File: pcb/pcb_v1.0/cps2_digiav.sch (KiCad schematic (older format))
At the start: 47 parts, among them U31 74LVC245, U32 74LVC245, U33 74LVC245, U34 SN74LVC3G17, U7 TC1262-3.3VDBTR, U8 TLV70033

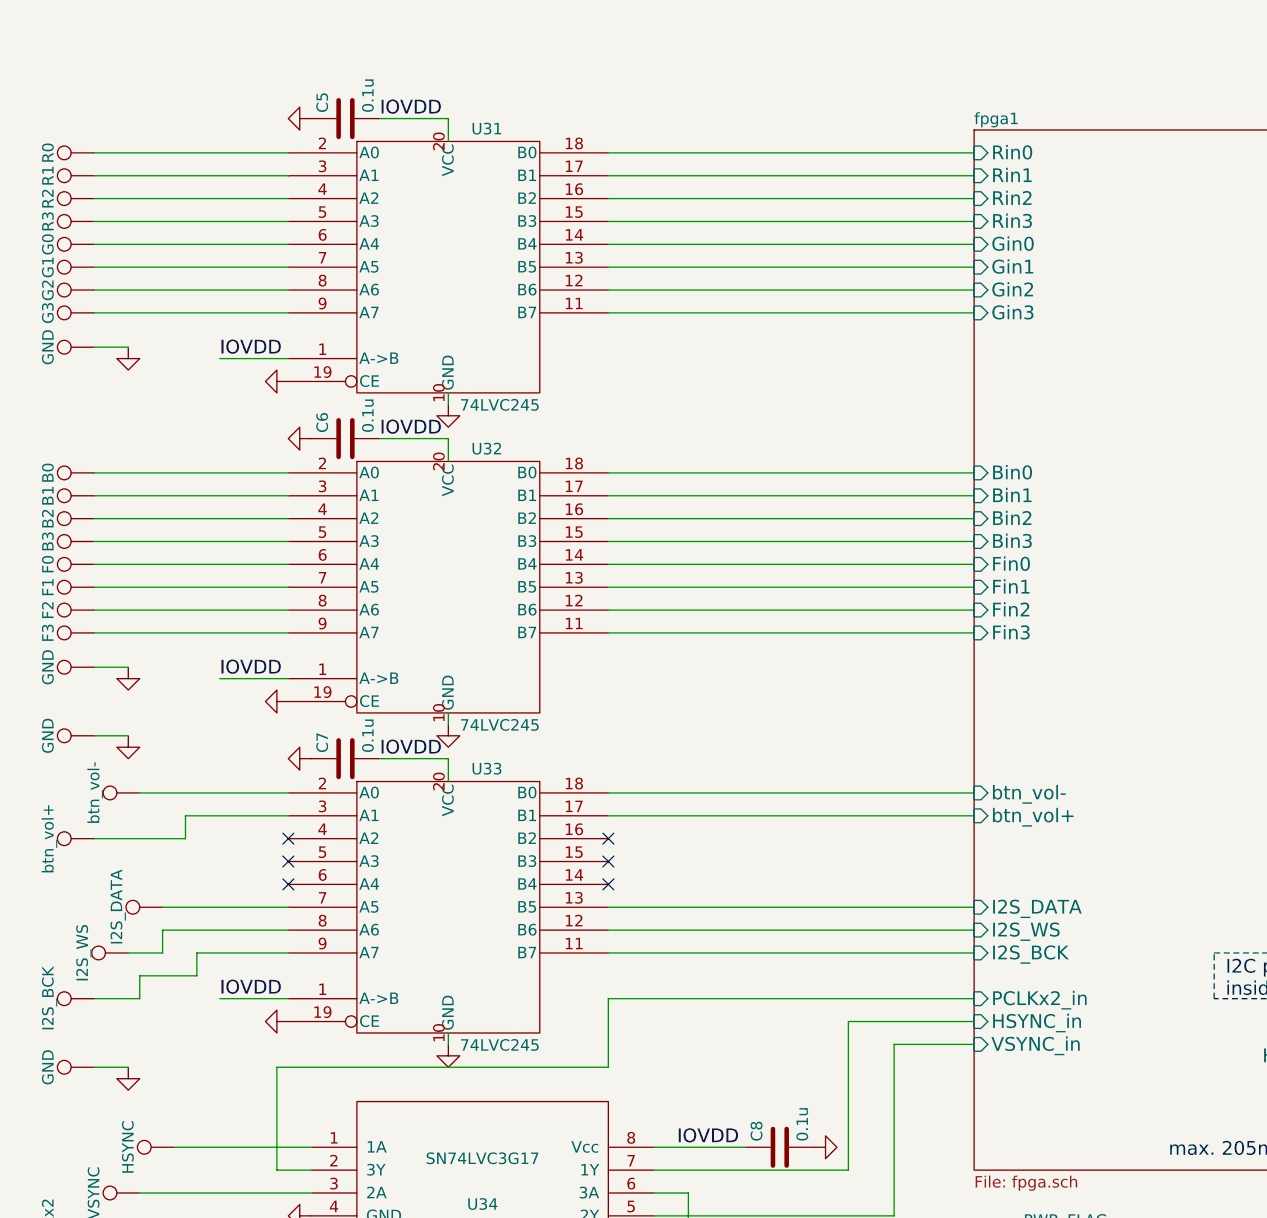
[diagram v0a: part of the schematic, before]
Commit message: Moved ICs to top, made to fit ontop of CPS2 DIPs
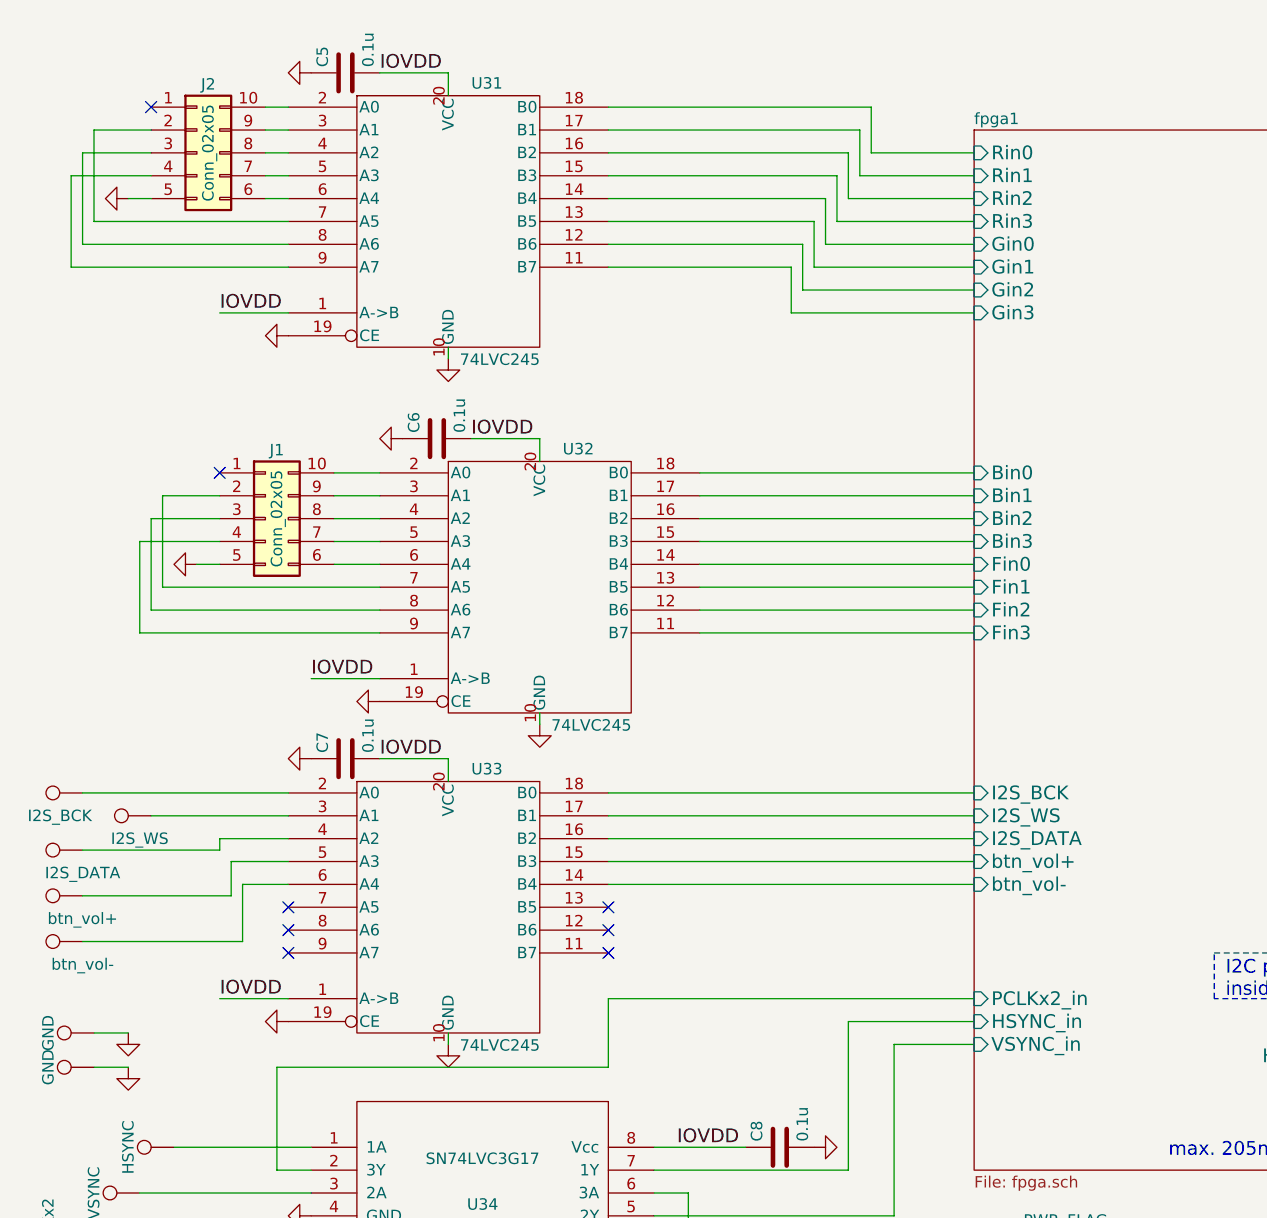
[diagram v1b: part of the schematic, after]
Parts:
- removed W10: G3, custom_components:SMD_PAD, symbol TEST_1P
- removed W11: B0, custom_components:SMD_PAD, symbol TEST_1P
- removed W12: B1, custom_components:SMD_PAD, symbol TEST_1P
- removed W13: B2, custom_components:SMD_PAD, symbol TEST_1P
- removed W14: B3, custom_components:SMD_PAD, symbol TEST_1P
- removed W15: F0, custom_components:SMD_PAD, symbol TEST_1P
- removed W16: F1, custom_components:SMD_PAD, symbol TEST_1P
- removed W17: F2, custom_components:SMD_PAD, symbol TEST_1P
- removed W18: F3, custom_components:SMD_PAD, symbol TEST_1P
- removed W27, W28: GND, custom_components:SMD_PAD, symbol TEST_1P
- removed W3: R0, custom_components:SMD_PAD, symbol TEST_1P
- removed W4: R1, custom_components:SMD_PAD, symbol TEST_1P
- removed W5: R2, custom_components:SMD_PAD, symbol TEST_1P
- removed W6: R3, custom_components:SMD_PAD, symbol TEST_1P
- removed W7: G0, custom_components:SMD_PAD, symbol TEST_1P
- removed W8: G1, custom_components:SMD_PAD, symbol TEST_1P
- removed W9: G2, custom_components:SMD_PAD, symbol TEST_1P
- added J1, J2: Conn_02x05, Housings_DIP:DIP-10_W7.62mm_LongPads, symbol Conn_02x05_Counter_Clockwise
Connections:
- net GND: now also J1.5 (Pin_5), J2.5 (Pin_5)
- net fpga1/I2S_BCK: now also U33.18 (B0); no longer U33.11 (B7)
- net fpga1/I2S_DATA: now also U33.16 (B2); no longer U33.13 (B5)
- net fpga1/I2S_WS: now also U33.17 (B1); no longer U33.12 (B6)
- net fpga1/btn_vol+: now also U33.15 (B3); no longer U33.17 (B1)
- net fpga1/btn_vol-: now also U33.14 (B4); no longer U33.18 (B0)
- net at U31.2 (A0): now also J2.10 (Pin_10)
- net at U31.3 (A1): now also J2.9 (Pin_9)
- net at U31.4 (A2): now also J2.8 (Pin_8)
- net at U31.5 (A3): now also J2.7 (Pin_7)
- net at U31.6 (A4): now also J2.6 (Pin_6)
- net at U31.7 (A5): now also J2.2 (Pin_2)
- net at U31.8 (A6): now also J2.3 (Pin_3)
- net at U31.9 (A7): now also J2.4 (Pin_4)
- net at U32.2 (A0): now also J1.10 (Pin_10)
- net at U32.3 (A1): now also J1.9 (Pin_9)
- net at U32.4 (A2): now also J1.8 (Pin_8)
- net at U32.5 (A3): now also J1.7 (Pin_7)
- net at U32.6 (A4): now also J1.6 (Pin_6)
- net at U32.7 (A5): now also J1.2 (Pin_2)
- net at U32.8 (A6): now also J1.3 (Pin_3)
- net at U32.9 (A7): now also J1.4 (Pin_4)
- net at U33.2 (A0): now also W20.1; no longer W23.1
- net at U33.3 (A1): now also W22.1; no longer W19.1
- net at U33.4 (A2): now also W25.1
- net at U33.5 (A3): now also W19.1
- net at U33.6 (A4): now also W23.1
- net at U33.7 (A5): no longer W25.1
- net at U33.8 (A6): no longer W22.1
- net at U33.9 (A7): no longer W20.1
- no-connect marks 6 -> 8
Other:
- moved on the sheet: C5, C6, U31, U32

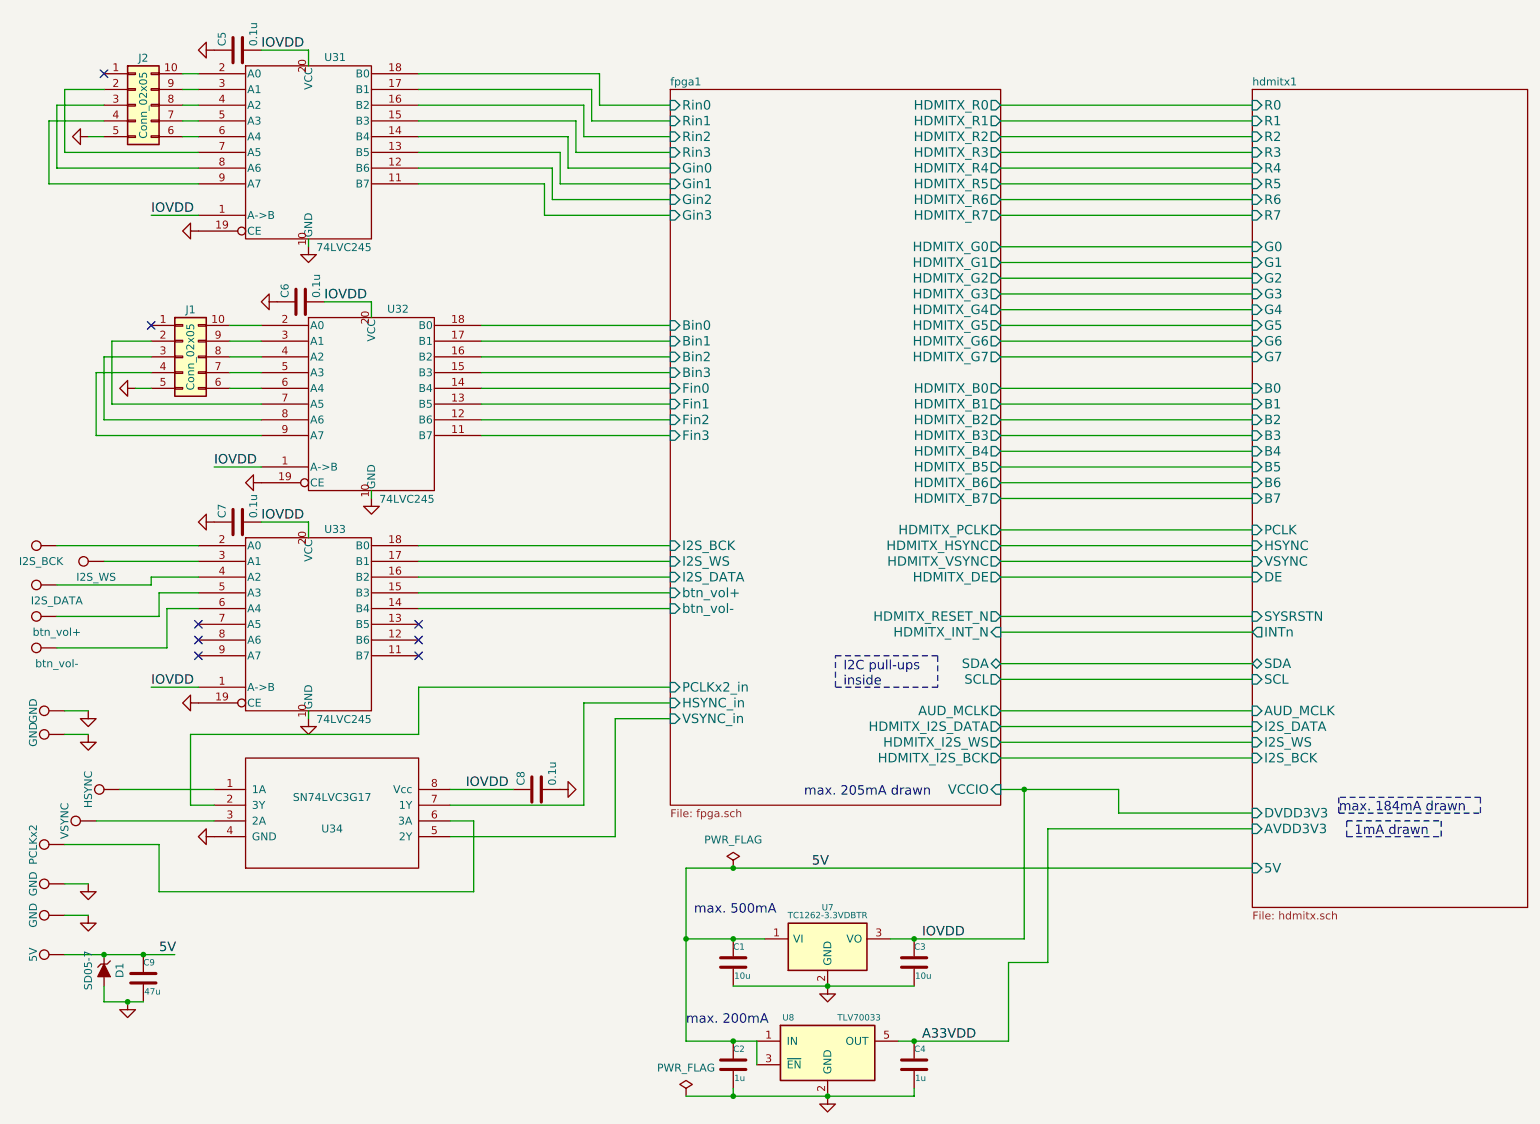
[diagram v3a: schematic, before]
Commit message: Added Si5351C
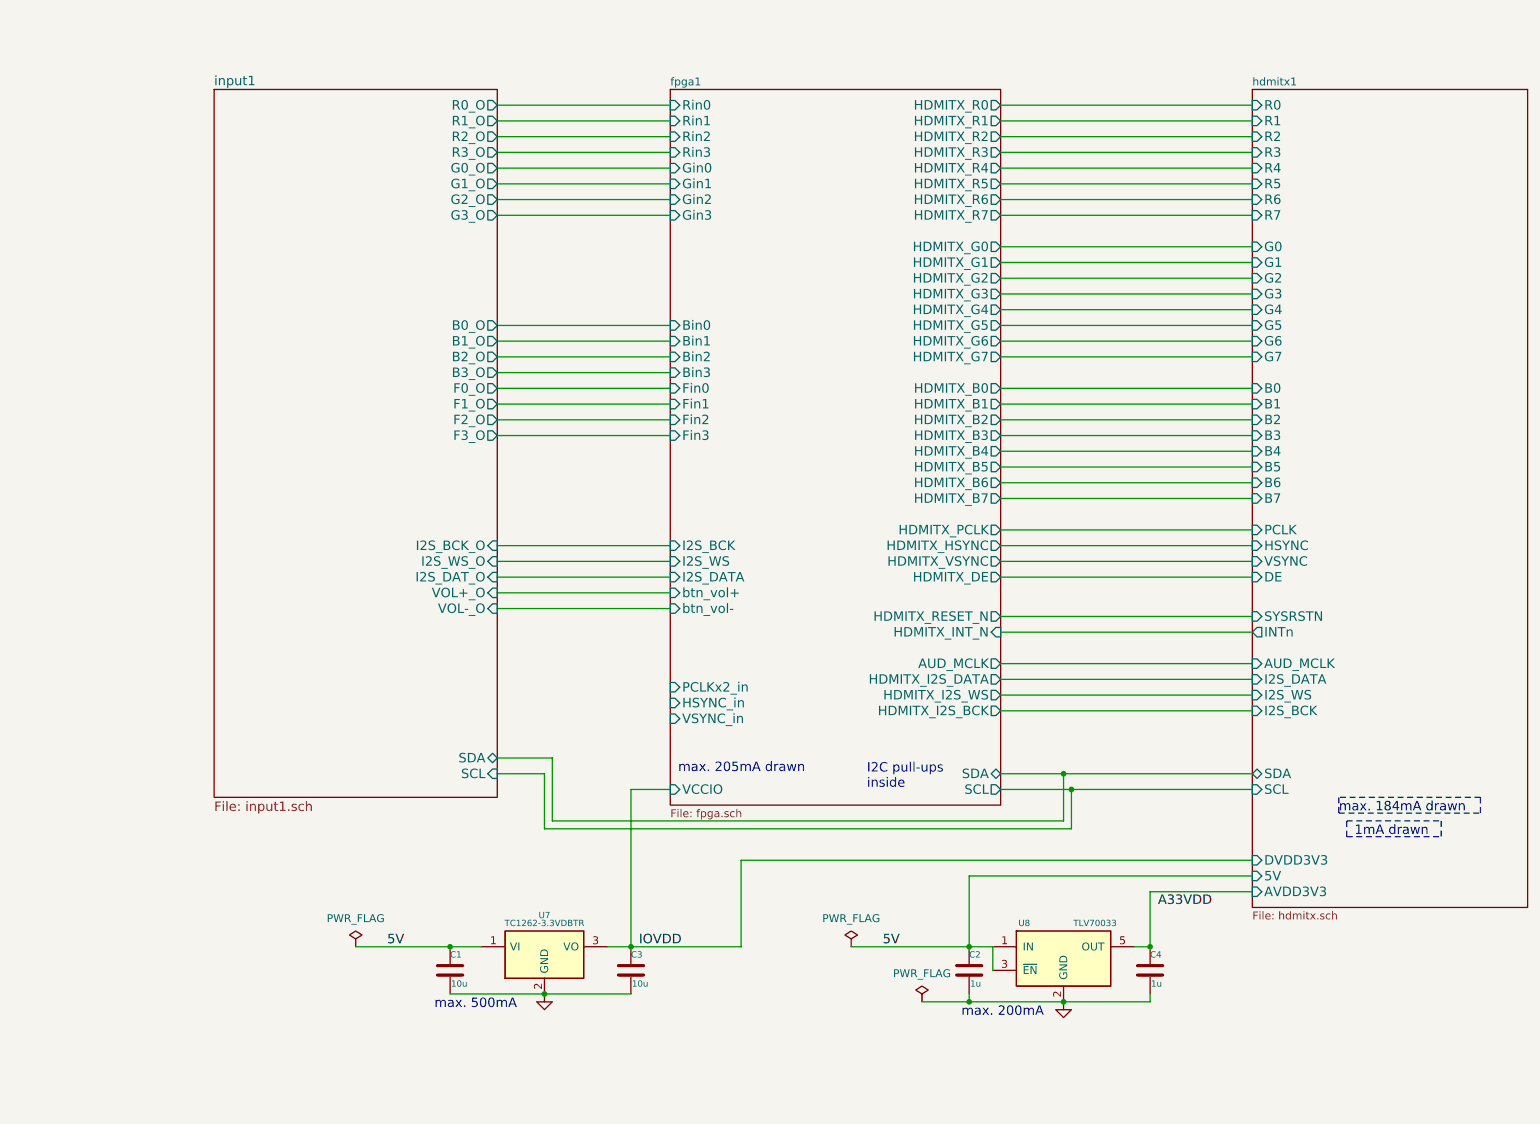
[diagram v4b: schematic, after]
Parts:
- removed C5, C6, C7, C8: 0.1u, custom_components:SM0603_Capa_libcms, symbol C
- removed C9: 47u, custom_components:SM0603_Capa_libcms, symbol C
- removed D1: SD05-7, custom_components:SOD-323_Handsoldering, symbol ZENERsmall
- removed J1, J2: Conn_02x05, Housings_DIP:DIP-10_W7.62mm_LongPads, symbol Conn_02x05_Counter_Clockwise
- removed U31, U32, U33: 74LVC245, custom_components:TSSOP-20_4.4x6.5mm_Pitch0.65mm_Handsoldering, symbol 74LVC245
- removed U34: SN74LVC3G17, custom_components:SSOP-8_3x3mm_Pitch0.65mm, symbol SN74LVC3G17
- removed W1: 5V, custom_components:SMD_PAD, symbol TEST_1P
- removed W19: btn_vol+, custom_components:SMD_PAD, symbol TEST_1P
- removed W2, W29, W30, W31: GND, custom_components:SMD_PAD, symbol TEST_1P
- removed W20: I2S_BCK, custom_components:SMD_PAD, symbol TEST_1P
- removed W21: PCLKx2, custom_components:SMD_PAD, symbol TEST_1P
- removed W22: I2S_WS, custom_components:SMD_PAD, symbol TEST_1P
- removed W23: btn_vol-, custom_components:SMD_PAD, symbol TEST_1P
- removed W24: VSYNC, custom_components:SMD_PAD, symbol TEST_1P
- removed W25: I2S_DATA, custom_components:SMD_PAD, symbol TEST_1P
- removed W26: HSYNC, custom_components:SMD_PAD, symbol TEST_1P
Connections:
- net A33VDD: no longer C4.1, U8.5 (OUT)
- new net hdmitx1/AVDD3V3: C4.1, U8.5 (OUT)
- no-connect marks 8 -> 0
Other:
- moved on the sheet: C1, C2, C3, C4, U7, U8
